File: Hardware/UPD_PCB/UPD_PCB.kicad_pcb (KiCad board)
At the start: 6 copper layers, 140 x 65 mm, 144 parts, among them IC1 STS30-DIS, J1 25A Fuse holder, J10 796739-2, J11 Conn_01x02, J12 Conn_01x01, J2 796739-2, J3 Conn_01x02, J4 1776119-2, J5 1776119-2, J6 1776119-2, J7 1776119-2, J8 1776119-2, J9 1776119-2, Q1 LMR51635XDDCR, Q2 LMR51635XDDCR, Q3 LMR51635XDDCR, Q4 LMR51635XDDCR, Q5 LMR51635XDDCR, Q6 LMR51635XDDCR, Q7 BSS84, U1 ACS711xEXLT-31AB, U2 INA219AxD, U3 INA219AxD, U4 INA219AxD, U5 INA219AxD, U6 INA219AxD, U7 INA219AxD

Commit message: Updated pcb
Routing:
- net GND: track 0.00 -> 6.63 mm, vias 0 -> 6
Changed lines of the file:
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@@
 	)
 	(segment
+		(start 157.8 65)
+		(end 157.8 66.042678)
+		(width 0.2)
+		(layer "F.Cu")
+		(net 1)
+	)
+	(segment
+		(start 187.75 65.00875)
+		(end 187.75 66.12625)
+		(width 0.2)
+		(layer "F.Cu")
+		(net 1)
+	)
+	(segment
+		(start 232.8375 65.00875)
+		(end 232.8375 66.12625)
+		(width 0.2)
+		(layer "F.Cu")
+		(net 1)
+	)
+	(segment
+		(start 217.75 65.01875)
+		(end 217.75 66.13625)
+		(width 0.2)
+		(layer "F.Cu")
+		(net 1)
+	)
+	(segment
+		(start 202.875001 65.00875)
+		(end 202.875001 66.12625)
+		(width 0.2)
+		(layer "F.Cu")
+		(net 1)
+	)
+	(segment
+		(start 172.75 65.00875)
+		(end 172.75 66.12625)
+		(width 0.2)
+		(layer "F.Cu")
+		(net 1)
+	)
+	(via
+		(at 202.875001 65.00875)
+		(size 0.55)
+		(drill 0.25)
+		(layers "F.Cu" "B.Cu")
+		(net 1)
+	)
+	(via
+		(at 157.8 65)
+		(size 0.55)
+		(drill 0.25)
+		(layers "F.Cu" "B.Cu")
+		(net 1)
+	)
+	(via
+		(at 217.75 65.01875)
+		(size 0.55)
+		(drill 0.25)
+		(layers "F.Cu" "B.Cu")
+		(net 1)
+	)
+	(via
+		(at 232.8375 65.00875)
+		(size 0.55)
+		(drill 0.25)
+		(layers "F.Cu" "B.Cu")
+		(net 1)
+	)
+	(via
+		(at 187.75 65.00875)
+		(size 0.55)
+		(drill 0.25)
+		(layers "F.Cu" "B.Cu")
+		(net 1)
+	)
+	(via
+		(at 172.75 65.00875)
+		(size 0.55)
+		(drill 0.25)
+		(layers "F.Cu" "B.Cu")
+		(net 1)
+	)
+	(segment
 		(start 125.312498 91.98)
 		(end 123.6675 91.98)
@@
 		(polygon
 			(pts
-				(xy 109.75 88) (xy 109.8 91.97) (xy 116.5 92) (xy 116.75 115) (xy 240 115) (xy 240 50) (xy 146.75 50)
+				(xy 109.75 88) (xy 109.8 91.97) (xy 116.5 92) (xy 116.75 115) (xy 240 115) (xy 240 86.051359) (xy 146.75 86.051359)
 				(xy 146.75 69.5) (xy 100 69.5) (xy 100 87.5) (xy 109.75 87.5)
 			)

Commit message: Final pcb before review
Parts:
- added REF**: OSHW-Logo_11.4x12mm_SilkScreen, Symbol:OSHW-Logo_11.4x12mm_SilkScreen, B.Cu at (230.7, 107.5)
- moved D6 14.9 mm to (217.0, 67.5)
- moved R50 14.9 mm to (217.0, 66.0)
- moved D7 14.9 mm to (202.1, 67.5)
- moved R51 14.9 mm to (202.1, 66.0)
- moved R54 1.60 mm to (114.2, 73.7)
- moved IC1 0.94 mm to (113.9, 76.8), turned to 180 degrees
- moved R53 0.80 mm to (117.6, 73.7)
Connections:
- D2 pad 2: +42V -> +42V_out
- J1 pad 2: Net-(J1-Pad2) -> +42V_out
- J1 pad 4: Net-(J1-Pad2) -> +42V_out
- J10 pad 2: Net-(J1-Pad2) -> +42V_out
- TP8 pad 1: Net-(J1-Pad2) -> +42V_out
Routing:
- net INA_SCL: track 23.6 -> 205.3 mm, vias 0 -> 10
- net INA_SDA: track 23.3 -> 193.7 mm, vias 0 -> 2
- net +5V_out: track 0.00 -> 104.6 mm, vias 11 -> 28
- net GND: track 6.63 -> 75.4 mm, vias 6 -> 58
- net Net-(U5-IN-): track 0.00 -> 8.30 mm
- net Net-(U2-IN-): track 0.00 -> 8.22 mm
- net Net-(U4-IN-): track 0.00 -> 8.16 mm
- net Net-(U3-IN-): track 0.00 -> 8.16 mm
- net Net-(U6-IN-): track 0.00 -> 8.01 mm
- net Net-(U7-IN-): track 0.00 -> 7.93 mm
- net Net-(U2-IN+): track 0.00 -> 6.76 mm
- net Net-(U7-IN+): track 0.00 -> 6.69 mm
- net Net-(U5-IN+): track 0.00 -> 6.55 mm
- net Net-(U3-IN+): track 0.00 -> 6.51 mm
- net Net-(U4-IN+): track 0.00 -> 6.47 mm
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- added copper zone on In3.Cu, net +19V_out
- added copper zone on B.Cu, net +42V_out
- added copper zone on In2.Cu, net +5V_out
- added copper zone on F.Cu, net GND
- removed copper zone on B.Cu, net Net-(J1-Pad2)

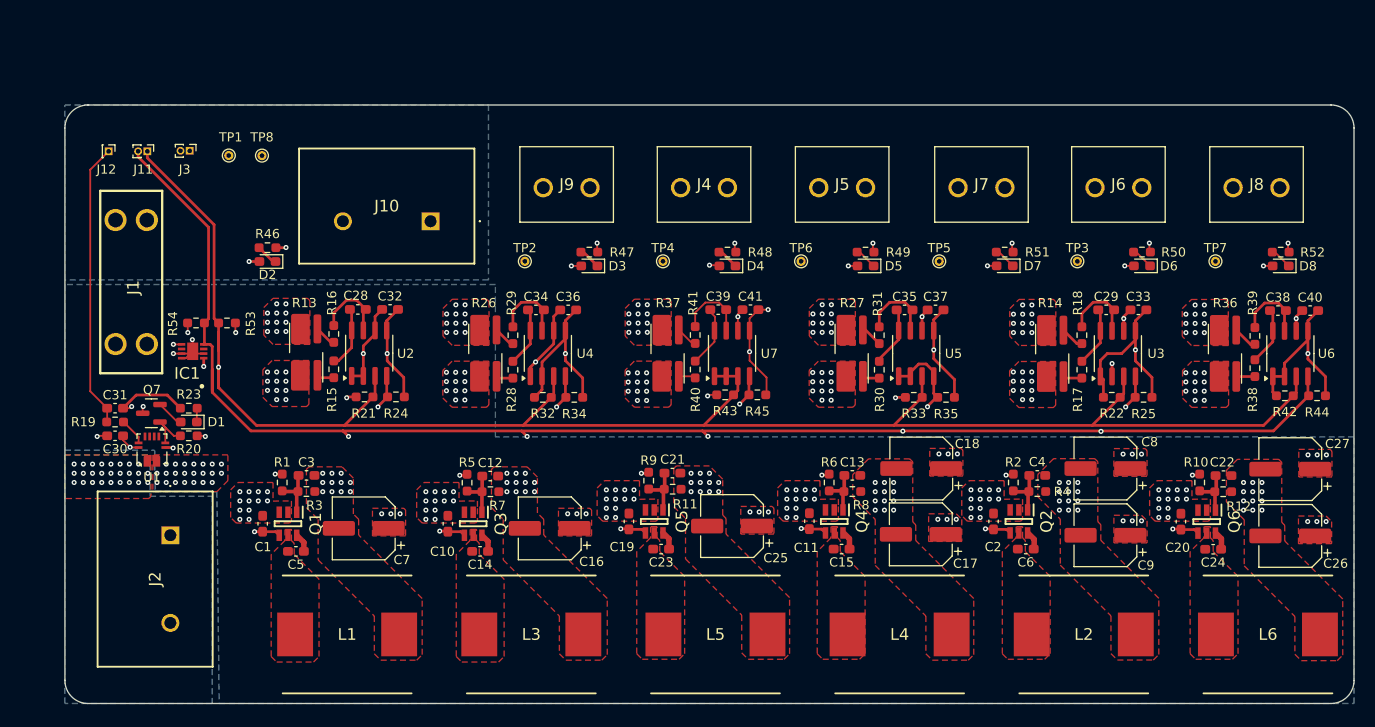
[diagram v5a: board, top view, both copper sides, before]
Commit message: Added silkscreen
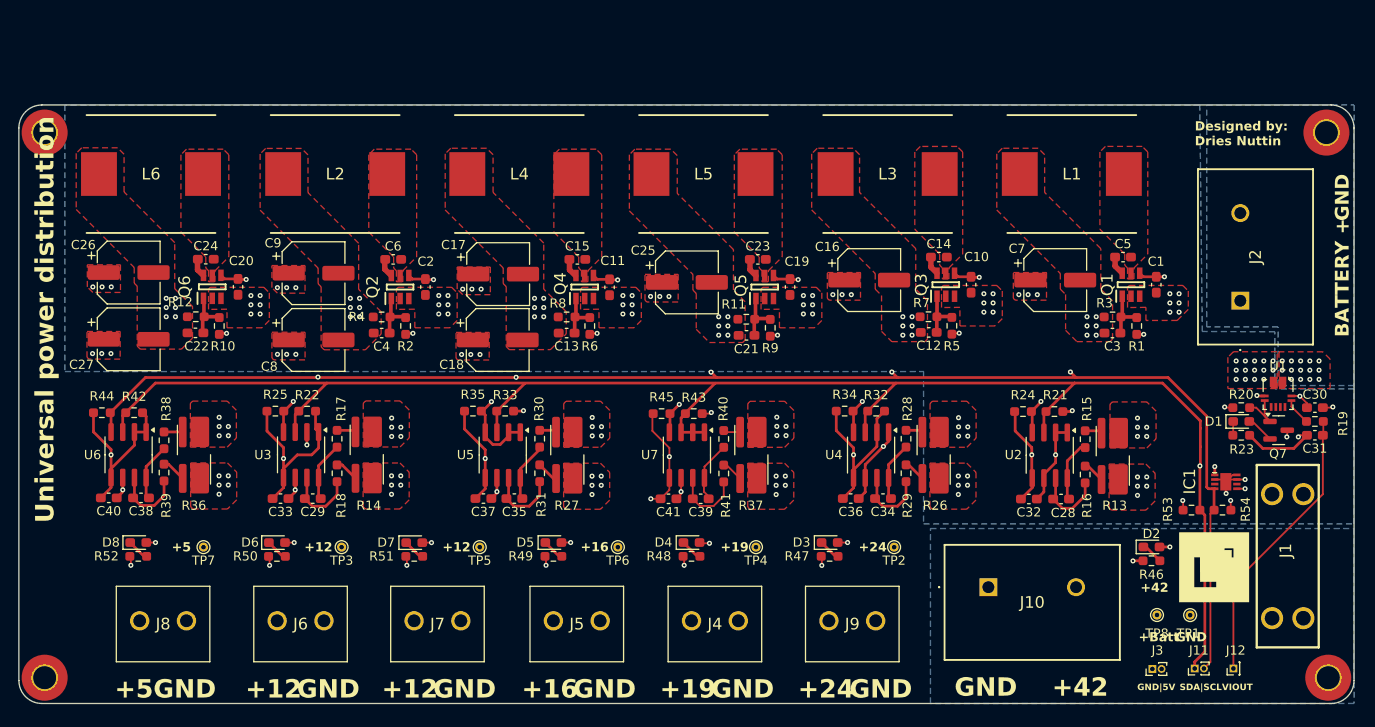
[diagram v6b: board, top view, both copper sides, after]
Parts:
- added G***: LOGO, Images:lapin_amk_round_logo, F.Cu at (224.8, 100.2)
- added G***: LOGO, Images:Lapin_amk_logo, B.Cu at (154.7, 67.6)
- added REF**: MountingHole_2.5mm_Pad_TopOnly, MountingHole:MountingHole_2.5mm_Pad_TopOnly, F.Cu at (97.8, 53.0)
- added REF**: MountingHole_2.5mm_Pad_TopOnly, MountingHole:MountingHole_2.5mm_Pad_TopOnly, F.Cu at (237.2, 112.2)
- added REF**: MountingHole_2.5mm_Pad_TopOnly, MountingHole:MountingHole_2.5mm_Pad_TopOnly, F.Cu at (97.8, 112.2)
- added REF**: MountingHole_2.5mm_Pad_TopOnly, MountingHole:MountingHole_2.5mm_Pad_TopOnly, F.Cu at (237.0, 53.0)
- moved J12 134.4 mm to (226.9, 111.2), turned to 90 degrees
- moved J8 132.5 mm to (108.1, 106.0), turned to 0 degrees
- moved C40 132.0 mm to (104.8, 92.7), turned to 180 degrees
- moved R44 132.0 mm to (104.0, 83.4), turned to 180 degrees
- moved L6 131.2 mm to (109.4, 57.5), turned to 180 degrees
- moved C30 130.3 mm to (235.7, 82.9), turned to 0 degrees
- moved C31 130.3 mm to (235.7, 85.9), turned to 180 degrees
- moved R19 130.3 mm to (235.7, 84.4), turned to 0 degrees
- moved C26 129.4 mm to (106.9, 68.2), turned to 0 degrees
- moved J1 129.1 mm to (232.8, 99.0), turned to -90 degrees
- moved R52 128.4 mm to (108.0, 99.0), turned to 0 degrees
- moved D8 127.7 mm to (108.0, 97.5), turned to 0 degrees
- moved C27 126.9 mm to (106.9, 75.5), turned to 0 degrees
- moved J11 126.9 mm to (222.7, 111.2), turned to 90 degrees
- moved U6 126.6 mm to (106.9, 88.0), turned to -90 degrees
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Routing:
- net INA_SDA: track 193.7 -> 188.5 mm
- net INA_SCL: track 205.3 -> 201.3 mm
- net +5V_out: vias 28 -> 22
- net +24V_out: vias 12 -> 6
- net +19V_out: vias 12 -> 6
- net +16V_out: vias 12 -> 6
- net +12V_2_out: vias 12 -> 6
- net +12V_1_out: vias 12 -> 6
- net IP+: vias 26 -> 14
- net +5V_NS: vias 23 -> 11
- net +42V: vias 94 -> 50
- net +24V: vias 22 -> 11
- net +19V: vias 22 -> 11
- net +16V: vias 22 -> 11
- net +12V_2: vias 23 -> 11
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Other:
- board size 140 x 65 mm -> 145 x 65 mm
- board text added: "+12"
- board text added: "+16"
- board text added: "+19"
- board text added: "+24"
- board text added: "+42"
- board text added: "+5"
- board text added: "+Batt"
- board text added: "3.5A max current delivery for each stage"
- board text added: "BATTERY +"
- board text added: "Designed by: Dries Nuttin"
- board text added: "GND"
- board text added: "GND|5V"
- board text added: "Max Rated Input Specs - 60 Volts - 31 Amp"
- board text added: "SDA|SCL"
- board text added: "Universal power distribution"
- board text added: "VIOUT"

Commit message: Updated pcb
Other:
- board text added: "0.0152mm"
- board text added: "0.035mm"
- board text added: "0.0994mm"
- board text added: "0.1088mm"
- board text added: "0.55mm"
- board text added: "L1 Sig"
- board text added: "L2 GND"
- board text added: "L3 Sig"
- board text added: "L4 PWR"
- board text added: "L5 GND"
- board text added: "L6 PWR"
- board text removed: "??? ??? ???"
- board text removed: "???mm"
- board text removed: "???mm (?oz)"
- board text removed: "ASSEMBLY NOTES (UNLESS OTHERWISE SPECIFIED) 1) DO NOT POPULATE PARTS ARE MARKED WITH A RED CROSS. 2) DO NOT POPULATE PARTS ARE NOT PRESENT IN THE BOM. 3) IF CONFLICTING INFORMATION IS FOUND BETWEEN THE ASSEMBLY FILE AND BOM, BOM SHOULD BE USED AS THE MAIN SOURCE."
- board text removed: "Back Side"
- board text removed: "Components"
- board text removed: "Front Side"
- board text removed: "L1 (Sig, PWR)"
- board text removed: "L2 (GND)"
- board text removed: "L3 (Sig, PWR)"
- board text removed: "L4 (Sig, PWR)"
- board text removed: "L5 (GND)"
- board text removed: "L6 (Sig, PWR)"
- board text removed: "THT SMD Total"
- board text removed: "Total"

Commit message: Finalized PCB
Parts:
- added G***: LOGO, Images:explosion_2, B.Cu at (223.8, 112.2)
- J11: value Conn_01x02 -> Conn_01x04; footprint Connector_PinHeader_1.00mm:PinHeader_1x02_P1.00mm_Vertical -> Connector:NS-Tech_Grove_1x04_P2mm_Vertical
- J12: value Conn_01x01 -> Conn_01x02; footprint Connector_PinHeader_1.00mm:PinHeader_1x01_P1.00mm_Vertical -> Connector_PinHeader_1.00mm:PinHeader_1x02_P1.00mm_Vertical
- moved TP1 124.2 mm to (98.0, 105.0), turned to -90 degrees
- moved J3 117.0 mm to (101.2, 105.0)
- moved REF** 101.9 mm to (109.4, 57.5)
- moved TP8 20.3 mm to (238.2, 100.2), turned to 90 degrees
- moved J11 4.89 mm to (219.0, 108.0)
- moved J12 3.88 mm to (230.8, 110.8)
- moved R33 0.20 mm to (148.0, 83.2)
- moved R43 0.12 mm to (168.3, 83.4)
- moved R45 0.12 mm to (164.8, 83.4)
- moved R32 0.11 mm to (188.2, 83.2)
- moved R24 0.11 mm to (204.0, 83.2)
- moved R34 0.09 mm to (184.6, 83.2)
- moved R21 0.07 mm to (207.4, 83.2)
- moved R25 0.06 mm to (122.9, 83.2)
- moved R22 0.05 mm to (126.3, 83.2)
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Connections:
- C16 pad 1: GND -> +19V
- C16 pad 2: +19V -> GND
- C17 pad 1: GND -> +12V_2
- C17 pad 2: +12V_2 -> GND
- C18 pad 1: GND -> +12V_2
- C18 pad 2: +12V_2 -> GND
- C25 pad 1: GND -> +16V
- C25 pad 2: +16V -> GND
- C26 pad 1: GND -> +5V_NS
- C26 pad 2: +5V_NS -> GND
- C27 pad 1: GND -> +5V_NS
- C27 pad 2: +5V_NS -> GND
- C7 pad 1: GND -> +24V
- C7 pad 2: +24V -> GND
- C8 pad 1: GND -> +12V_1
- C8 pad 2: +12V_1 -> GND
- C9 pad 1: GND -> +12V_1
- C9 pad 2: +12V_1 -> GND
- J11 pad 1: INA_SDA -> GND
- J11 pad 2: INA_SCL -> +5V_out
- J12 pad 1: VIOUT -> GND
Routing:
- net INA_SDA: track 188.5 -> 185.1 mm
- net VIOUT: track 30.9 -> 28.4 mm
- net INA_SCL: track 201.3 -> 199.4 mm
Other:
- board text added: "Exploding Robotics Association"
- board text added: "Universal power distribution V1.0"
- board text removed: "Universal power distribution"
